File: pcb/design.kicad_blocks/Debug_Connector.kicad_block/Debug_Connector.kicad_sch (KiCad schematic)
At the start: 1 part, among them J5 Debug

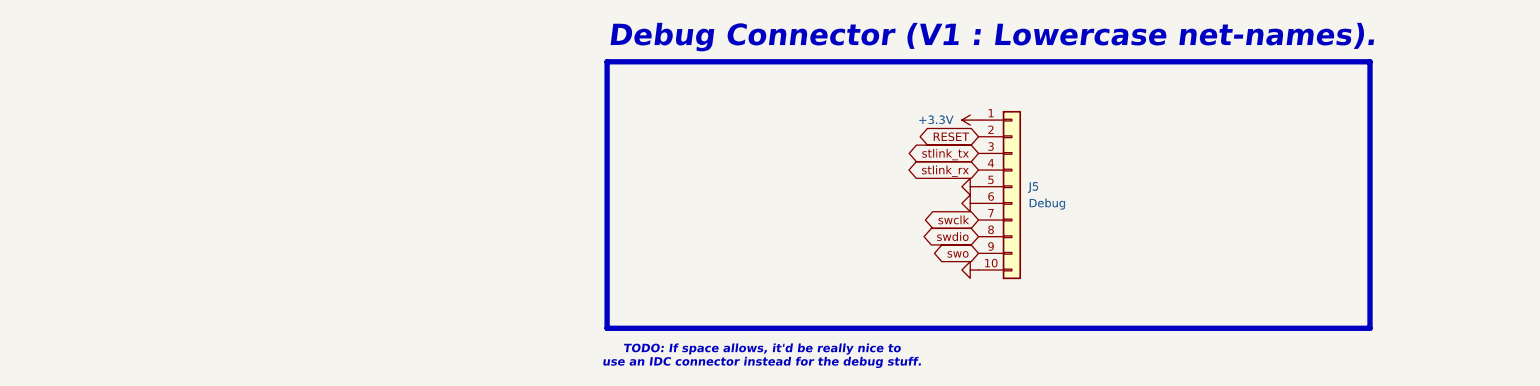
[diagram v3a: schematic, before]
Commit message: `Debug Connector (V2 : Removed To-Do).`
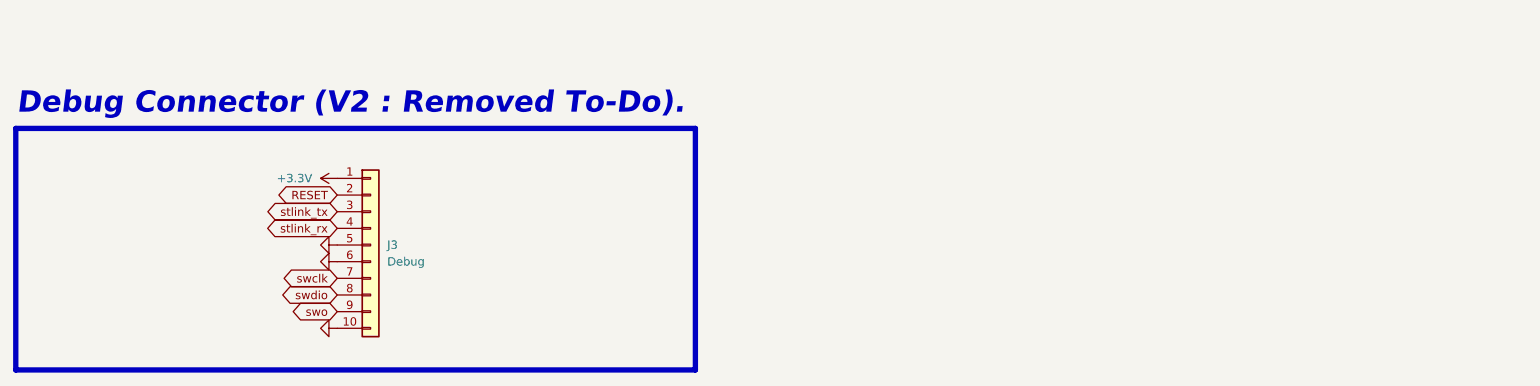
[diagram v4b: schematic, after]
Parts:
- renumbered J5 to J3
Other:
- note added: "Debug Connector (V2 : Removed To-Do)."
- note removed: "Debug Connector (V1 : Lowercase net-names)."
- note removed: "TODO: If space allows, it'd be really nice to use an IDC connector instead for the debug stuff."
- moved on the sheet: J3
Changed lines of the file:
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@@
 	(paper "A4")
 	(rectangle
-		(start 441.198 210.82)
-		(end 557.53 251.46)
+		(start 351.028 220.98)
+		(end 454.66 257.81)
 		(stroke
 			(width 0.8128)
@@
 		)
 	)
-	(text "Debug Connector (V1 : Lowercase net-names)."
-		(exclude_from_sim no)
-		(at 441.325 208.915 0)
+	(text "Debug Connector (V2 : Removed To-Do)."
+		(exclude_from_sim no)
+		(at 351.155 219.075 0)
 		(effects
 			(font
@@
 		)
 	)
-	(text "TODO: If space allows, it'd be really nice to\nuse an IDC connector instead for the debug stuff."
-		(exclude_from_sim no)
-		(at 464.82 255.778 0)
-		(effects
-			(font
-				(size 1.27 1.27)
-				(thickness 0.254)
-				(bold yes)
-				(italic yes)
-				(color 255 0 255 1)
-			)
-		)
-	)
 	(global_label "swo"
 		(shape bidirectional)
-		(at 497.84 240.03 180)
-		(fields_autoplaced yes)
-		(effects
-			(font
-				(size 1.27 1.27)
-			)
-			(justify right)
-		)
-		(property "Intersheetrefs" "${INTERSHEET_REFS}"
-			(at 490.2359 240.03 0)
+		(at 400.05 248.92 180)
+		(fields_autoplaced yes)
+		(effects
+			(font
+				(size 1.27 1.27)
+			)
+			(justify right)
+		)
+		(property "Intersheetrefs" "${INTERSHEET_REFS}"
+			(at 392.4459 248.92 0)
 			(effects
 				(font
@@
 	(global_label "RESET"
 		(shape bidirectional)
-		(at 497.84 222.25 180)
-		(fields_autoplaced yes)
-		(effects
-			(font
-				(size 1.27 1.27)
-			)
-			(justify right)
-		)
-		(property "Intersheetrefs" "${INTERSHEET_REFS}"
-			(at 487.9984 222.25 0)
+		(at 400.05 231.14 180)
+		(fields_autoplaced yes)
+		(effects
+			(font
+				(size 1.27 1.27)
+			)
+			(justify right)
+		)
+		(property "Intersheetrefs" "${INTERSHEET_REFS}"
+			(at 390.2084 231.14 0)
 			(effects
 				(font
@@
 	(global_label "swclk"
 		(shape bidirectional)
-		(at 497.84 234.95 180)
-		(fields_autoplaced yes)
-		(effects
-			(font
-				(size 1.27 1.27)
-			)
-			(justify right)
-		)
-		(property "Intersheetrefs" "${INTERSHEET_REFS}"
-			(at 488.603 234.95 0)
+		(at 400.05 243.84 180)
+		(fields_autoplaced yes)
+		(effects
+			(font
+				(size 1.27 1.27)
+			)
+			(justify right)
+		)
+		(property "Intersheetrefs" "${INTERSHEET_REFS}"
+			(at 390.813 243.84 0)
 			(effects
 				(font
@@
 	(global_label "stlink_tx"
 		(shape bidirectional)
-		(at 497.84 224.79 180)
-		(fields_autoplaced yes)
-		(effects
-			(font
-				(size 1.27 1.27)
-			)
-			(justify right)
-		)
-		(property "Intersheetrefs" "${INTERSHEET_REFS}"
-			(at 485.8212 224.79 0)
+		(at 400.05 233.68 180)
+		(fields_autoplaced yes)
+		(effects
+			(font
+				(size 1.27 1.27)
+			)
+			(justify right)
+		)
+		(property "Intersheetrefs" "${INTERSHEET_REFS}"
+			(at 388.0312 233.68 0)
 			(effects
 				(font
@@
 	(global_label "swdio"
 		(shape bidirectional)
-		(at 497.84 237.49 180)
-		(fields_autoplaced yes)
-		(effects
-			(font
-				(size 1.27 1.27)
-			)
-			(justify right)
-		)
-		(property "Intersheetrefs" "${INTERSHEET_REFS}"
-			(at 488.4821 237.49 0)
+		(at 400.05 246.38 180)
+		(fields_autoplaced yes)
+		(effects
+			(font
+				(size 1.27 1.27)
+			)
+			(justify right)
+		)
+		(property "Intersheetrefs" "${INTERSHEET_REFS}"
+			(at 390.6921 246.38 0)
 			(effects
 				(font
@@
 	(global_label "stlink_rx"
 		(shape bidirectional)
-		(at 497.84 227.33 180)
-		(fields_autoplaced yes)
-		(effects
-			(font
-				(size 1.27 1.27)
-			)
-			(justify right)
-		)
-		(property "Intersheetrefs" "${INTERSHEET_REFS}"
-			(at 485.7607 227.33 0)
+		(at 400.05 236.22 180)
+		(fields_autoplaced yes)
+		(effects
+			(font
+				(size 1.27 1.27)
+			)
+			(justify right)
+		)
+		(property "Intersheetrefs" "${INTERSHEET_REFS}"
+			(at 387.9707 236.22 0)
 			(effects
 				(font
@@
 	(symbol
 		(lib_id "power:+3.3V")
-		(at 497.84 219.71 90)
+		(at 400.05 228.6 90)
 		(unit 1)
 		(exclude_from_sim no)
@@
 		(dnp no)
 		(fields_autoplaced yes)
-		(property "Reference" "#PWR012"
-			(at 501.65 219.71 0)
+		(property "Reference" "#PWR044"
+			(at 403.86 228.6 0)
 			(effects
 				(font
@@
 		)
 		(property "Value" "+3.3V"
-			(at 494.03 219.7099 90)
+			(at 396.24 228.5999 90)
 			(effects
 				(font
@@
 		)
 		(property "Footprint" ""
-			(at 497.84 219.71 0)
+			(at 400.05 228.6 0)
 			(effects
 				(font
@@
 		)
 		(property "Datasheet" ""
-			(at 497.84 219.71 0)
+			(at 400.05 228.6 0)
 			(effects
 				(font
@@
 		)
 		(property "Description" "Power symbol creates a global label with name \"+3.3V\""
-			(at 497.84 219.71 0)
+			(at 400.05 228.6 0)
 			(effects
 				(font
@@
 			(project ""
 				(path "/0a179c33-cb18-4019-99e7-0e00d41f97d6"
-					(reference "#PWR012")
+					(reference "#PWR044")
 					(unit 1)
 				)
@@
 	(symbol
 		(lib_id "Connector_Generic:Conn_01x10")
-		(at 502.92 229.87 0)
+		(at 405.13 238.76 0)
 		(unit 1)
 		(exclude_from_sim no)
@@
 		(dnp no)
 		(fields_autoplaced yes)
-		(property "Reference" "J5"
-			(at 505.46 229.8699 0)
+		(property "Reference" "J3"
+			(at 407.67 238.7599 0)
 			(effects
 				(font
@@
 		)
 		(property "Value" "Debug"
-			(at 505.46 232.4099 0)
+			(at 407.67 241.2999 0)
 			(effects
 				(font
@@
 		)
 		(property "Footprint" "pcb:Molex_PicoBlade_53047-1010_1x10_P1.25mm_Vertical"
-			(at 502.92 229.87 0)
+			(at 405.13 238.76 0)
 			(effects
 				(font
@@
 		)
 		(property "Datasheet" "~"
-			(at 502.92 229.87 0)
+			(at 405.13 238.76 0)
 			(effects
 				(font
@@
 		)
 		(property "Description" "Generic connector, single row, 01x10, script generated (kicad-library-utils/schlib/autogen/connector/)"
-			(at 502.92 229.87 0)
+			(at 405.13 238.76 0)
 			(effects
 				(font
@@
 			(project ""
 				(path "/0a179c33-cb18-4019-99e7-0e00d41f97d6"
-					(reference "J5")
+					(reference "J3")
 					(unit 1)
 				)
@@
 	(symbol
 		(lib_id "power:GND")
-		(at 497.84 242.57 270)
+		(at 400.05 251.46 270)
 		(mirror x)
 		(unit 1)
@@
 		(dnp no)
 		(fields_autoplaced yes)
-		(property "Reference" "#PWR017"
-			(at 491.49 242.57 0)
+		(property "Reference" "#PWR047"
+			(at 393.7 251.46 0)
 			(effects
 				(font
@@
 		)
 		(property "Value" "GND"
-			(at 494.03 242.5699 90)
+			(at 396.24 251.4599 90)
 			(effects
 				(font
@@
 		)
 		(property "Footprint" ""
-			(at 497.84 242.57 0)
+			(at 400.05 251.46 0)
 			(effects
 				(font
@@
 		)
 		(property "Datasheet" ""
-			(at 497.84 242.57 0)
+			(at 400.05 251.46 0)
 			(effects
 				(font
@@
 		)
 		(property "Description" "Power symbol creates a global label with name \"GND\" , ground"
-			(at 497.84 242.57 0)
+			(at 400.05 251.46 0)
 			(effects
 				(font
@@
 			(project ""
 				(path "/0a179c33-cb18-4019-99e7-0e00d41f97d6"
-					(reference "#PWR017")
+					(reference "#PWR047")
 					(unit 1)
 				)
@@
 	(symbol
 		(lib_id "power:GND")
-		(at 497.84 229.87 270)
+		(at 400.05 238.76 270)
 		(unit 1)
 		(exclude_from_sim no)
@@
 		(dnp no)
 		(fields_autoplaced yes)
-		(property "Reference" "#PWR013"
-			(at 491.49 229.87 0)
+		(property "Reference" "#PWR045"
+			(at 393.7 238.76 0)
 			(effects
 				(font
@@
 		)
 		(property "Value" "GND"
-			(at 494.03 229.8701 90)
+			(at 396.24 238.7601 90)
 			(effects
 				(font
@@
 		)
 		(property "Footprint" ""
-			(at 497.84 229.87 0)
+			(at 400.05 238.76 0)
 			(effects
 				(font
@@
 		)
 		(property "Datasheet" ""
-			(at 497.84 229.87 0)
+			(at 400.05 238.76 0)
 			(effects
 				(font
@@
 		)
 		(property "Description" "Power symbol creates a global label with name \"GND\" , ground"
-			(at 497.84 229.87 0)
+			(at 400.05 238.76 0)
 			(effects
 				(font
@@
 			(project ""
 				(path "/0a179c33-cb18-4019-99e7-0e00d41f97d6"
-					(reference "#PWR013")
+					(reference "#PWR045")
 					(unit 1)
 				)
@@
 	(symbol
 		(lib_id "power:GND")
-		(at 497.84 232.41 270)
+		(at 400.05 241.3 270)
 		(mirror x)
 		(unit 1)
@@
 		(dnp no)
 		(fields_autoplaced yes)
-		(property "Reference" "#PWR016"
-			(at 491.49 232.41 0)
+		(property "Reference" "#PWR046"
+			(at 393.7 241.3 0)
 			(effects
 				(font
@@
 		)
 		(property "Value" "GND"
-			(at 494.03 232.4099 90)
+			(at 396.24 241.2999 90)
 			(effects
 				(font
@@
 		)
 		(property "Footprint" ""
-			(at 497.84 232.41 0)
+			(at 400.05 241.3 0)
 			(effects
 				(font
@@
 		)
 		(property "Datasheet" ""
-			(at 497.84 232.41 0)
+			(at 400.05 241.3 0)
 			(effects
 				(font
@@
 		)
 		(property "Description" "Power symbol creates a global label with name \"GND\" , ground"
-			(at 497.84 232.41 0)
+			(at 400.05 241.3 0)
 			(effects
 				(font
@@
 			(project ""
 				(path "/0a179c33-cb18-4019-99e7-0e00d41f97d6"
-					(reference "#PWR016")
+					(reference "#PWR046")
 					(unit 1)
 				)
